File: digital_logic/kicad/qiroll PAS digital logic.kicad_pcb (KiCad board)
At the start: 2 copper layers, 26 parts, among them J1 led_sw1, J2 mode_thr_batt, J3 pas_sense, U1 14538, U2 4023, U3 4027, U4 14538, U5 L7805

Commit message: pcb version 1, new features
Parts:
- added C12: .1u, Capacitor_SMD:C_0603_1608Metric, F.Cu at (150.5, 55.9)
- added C13: .1u, Capacitor_SMD:C_0603_1608Metric, F.Cu at (144.8, 78.7)
- added H1: MountingHole_Pad, MountingHole:MountingHole_2.2mm_M2_DIN965_Pad, F.Cu at (162.1, 45.2)
- added H2: MountingHole_Pad, MountingHole:MountingHole_2.2mm_M2_DIN965_Pad, F.Cu at (113.8, 45.2)
- added H3: MountingHole_Pad, MountingHole:MountingHole_2.2mm_M2_DIN965_Pad, F.Cu at (162.1, 85.9)
- added H4: MountingHole_Pad, MountingHole:MountingHole_2.2mm_M2_DIN965_Pad, F.Cu at (113.8, 85.9)
- added J4: brk_sense, Connector_PinHeader_2.54mm:PinHeader_1x02_P2.54mm_Vertical, F.Cu at (156.8, 53.3)
- added J5: jumper, Connector_PinHeader_2.54mm:PinHeader_2x02_P2.54mm_Vertical, F.Cu at (133.3, 59.7)
- added R10: 1.6k, Resistor_SMD:R_0603_1608Metric, F.Cu at (118.7, 56.5)
- added R8: 100k, Resistor_SMD:R_0603_1608Metric, F.Cu at (117.5, 82.5)
- added R9: 392K, Resistor_SMD:R_0603_1608Metric, F.Cu at (131.4, 73.7)
- added U6: 4081, Package_SO:SOIC-14_3.9x8.7mm_P1.27mm, F.Cu at (144.8, 62.2)
- added U7: 4047, Package_SO:SOIC-14_3.9x8.7mm_P1.27mm, F.Cu at (124.5, 79.4)
- added U8: 74VHC1G32, Package_SO:TSOP-5_1.65x3.05mm_P0.95mm, F.Cu at (125.0, 68.6)
- C10: value .1u -> 0.47u
- C11: value .1u -> 1u
- C3, C4, C5: footprint Capacitor_SMD:C_0201_0603Metric -> Capacitor_SMD:C_0603_1608Metric
- C7: value 0.1u -> .1u
- C9: value 150u -> 200u; footprint Capacitor_THT:CP_Radial_D5.0mm_P2.00mm -> Capacitor_THT:CP_Radial_D6.3mm_P2.50mm
- J2: footprint Connector_Molex:Molex_KK-254_AE-6410-04A_1x04_P2.54mm_Vertical -> Connector_PinHeader_2.54mm:PinHeader_1x04_P2.54mm_Vertical
- J3: footprint Connector_Molex:Molex_KK-254_AE-6410-03A_1x03_P2.54mm_Vertical -> Connector_PinHeader_2.54mm:PinHeader_1x03_P2.54mm_Vertical
- U1, U3, U4: footprint Package_SO:TSSOP-16_4.4x5mm_P0.65mm -> Package_SO:SOIC-16_3.9x9.9mm_P1.27mm
- U2: footprint Package_SO:TSSOP-14_4.4x5mm_P0.65mm -> Package_SO:SOIC-14_3.9x8.7mm_P1.27mm
- moved C10 74.4 mm to (117.5, 78.1), turned to 180 degrees
- moved R3 62.0 mm to (141.6, 56.5)
- moved C11 59.4 mm to (131.4, 70.5), turned to 180 degrees
- moved R1 54.1 mm to (153.7, 56.5)
- moved C1 49.2 mm to (158.8, 56.5)
- moved R7 48.5 mm to (144.8, 80.6)
- moved U4 44.7 mm to (156.2, 78.7)
- moved R2 43.9 mm to (153.7, 71.1)
- moved R5 42.8 mm to (148.6, 80.6), turned to 180 degrees
- moved R6 42.5 mm to (158.8, 71.1)
- moved U2 41.7 mm to (134.0, 79.4), turned to 180 degrees
- moved U1 39.5 mm to (156.2, 62.9)
- moved R4 39.5 mm to (148.6, 83.2), turned to 180 degrees
- moved C4 38.8 mm to (158.8, 69.2), turned to 180 degrees
- moved C9 37.2 mm to (121.9, 60.3)
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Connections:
- C10 pad 1: GND -> Net-(C10-Pad1)
- C10 pad 2: VDD -> Net-(C10-Pad2)
- C11 pad 2: VDD -> Net-(C11-Pad2)
- C7 pad 1: VDD -> VCC
- C9 pad 1: VDD -> VCC
- J2 pad 2: Net-(C6-Pad1) -> Net-(J2-Pad2)
- J3 pad 1: VDD -> VCC
- R1 pad 1: VDD -> VCC
- R2 pad 1: VDD -> VCC
- R3 pad 1: VDD -> VCC
- R4 pad 1: VDD -> VCC
- R5 pad 1: VDD -> VCC
- R6 pad 1: VDD -> VCC
- U1 pad 13: VDD -> VCC
- U1 pad 16: VDD -> VCC
- U1 pad 3: VDD -> VCC
- U1 pad 5: VDD -> VCC
- U2 pad 1: Net-(U1-Pad10) -> Net-(U2-Pad1)
- U2 pad 10: Net-(U2-Pad10) -> Net-(U2-Pad1)
- U2 pad 11: Net-(J2-Pad3) -> BRK
- U2 pad 12: Net-(J2-Pad3) -> BRK
- U2 pad 13: Net-(J2-Pad3) -> BRK
- U2 pad 14: VDD -> VCC
- U2 pad 2: Net-(U1-Pad6) -> PEDAL
- U2 pad 8: Net-(J1-Pad3) -> PAS_ON
- U2 pad 9: Net-(J2-Pad3) -> Net-(R9-Pad2)
- U3 pad 1: Net-(J1-Pad3) -> PAS_ON
- U3 pad 10: VDD -> VCC
- U3 pad 11: VDD -> VCC
- U3 pad 12: Net-(U2-Pad10) -> PEDAL
- U3 pad 14: Net-(J2-Pad4) -> Net-(J5-Pad4)
- U3 pad 16: VDD -> VCC
- U3 pad 2: Net-(U3-Pad2) -> PAS_OFF
- U3 pad 5: VDD -> VCC
- U3 pad 6: VDD -> VCC
- U3 pad 9: GND -> BRK
- U4 pad 11: VDD -> VCC
- U4 pad 13: VDD -> VCC
- U4 pad 16: VDD -> VCC
- U4 pad 3: VDD -> VCC
- U5 pad 3: VDD -> VCC
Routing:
- net VCC: track 0.00 -> 241.8 mm, vias 0 -> 12
- net Net-(J1-Pad2): track 0.00 -> 85.7 mm, vias 0 -> 2
- net GND: track 0.00 -> 74.6 mm, vias 0 -> 18
- net PAS_OFF: track 0.00 -> 58.5 mm, vias 0 -> 6
- net Net-(U6-Pad3): track 0.00 -> 57.2 mm, vias 0 -> 4
- net BRK: track 0.00 -> 57.0 mm, vias 0 -> 4
- net Net-(U1-Pad10): track 0.00 -> 54.9 mm, vias 0 -> 2
- net Net-(J3-Pad3): track 0.00 -> 43.3 mm
- net RGN_FLSH: track 0.00 -> 39.6 mm, vias 0 -> 2
- net Net-(U2-Pad1): track 0.00 -> 39.5 mm, vias 0 -> 4
- net Net-(U6-Pad13): track 0.00 -> 35.0 mm, vias 0 -> 2
- net PAS_ON: track 0.00 -> 34.4 mm, vias 0 -> 2
- net PEDAL: track 0.00 -> 32.8 mm, vias 0 -> 4
- net Net-(J2-Pad3): track 0.00 -> 32.5 mm
- net Net-(U2-Pad5): track 0.00 -> 31.7 mm
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- added copper zone on B.Cu, net GND
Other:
- board outline added: 53.3 x 45.7 mm
- board text added: "+5v"
- board text added: "batt_in"
- board text added: "brk"
- board text added: "btn"
- board text added: "gnd"
- board text added: "led"
- board text added: "pedal"
- board text added: "pro/std"
- board text added: "qiroll pedal assist v1 Eric Dasmalchi"
- board text added: "rgn/ mode"
- board text added: "throttle"

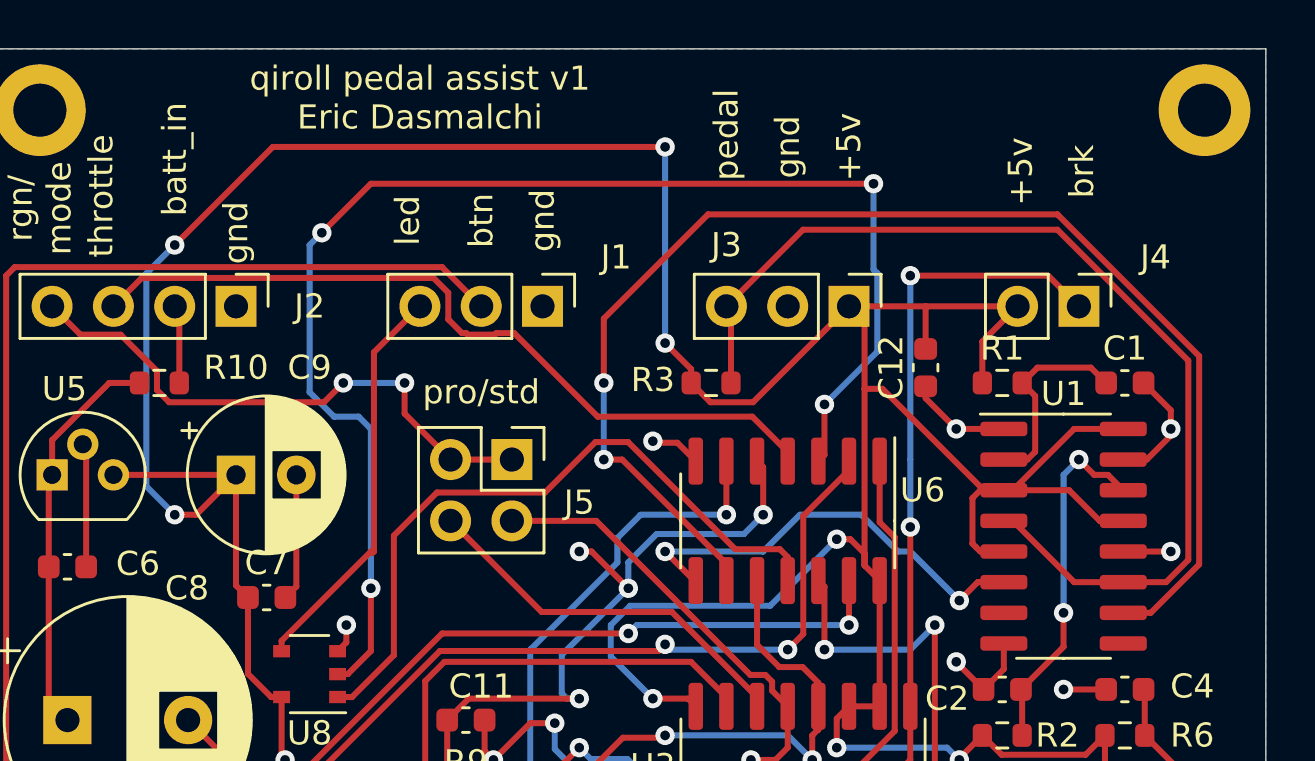
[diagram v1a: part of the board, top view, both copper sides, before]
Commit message: add brake sensor pulldown, incomplete BOM
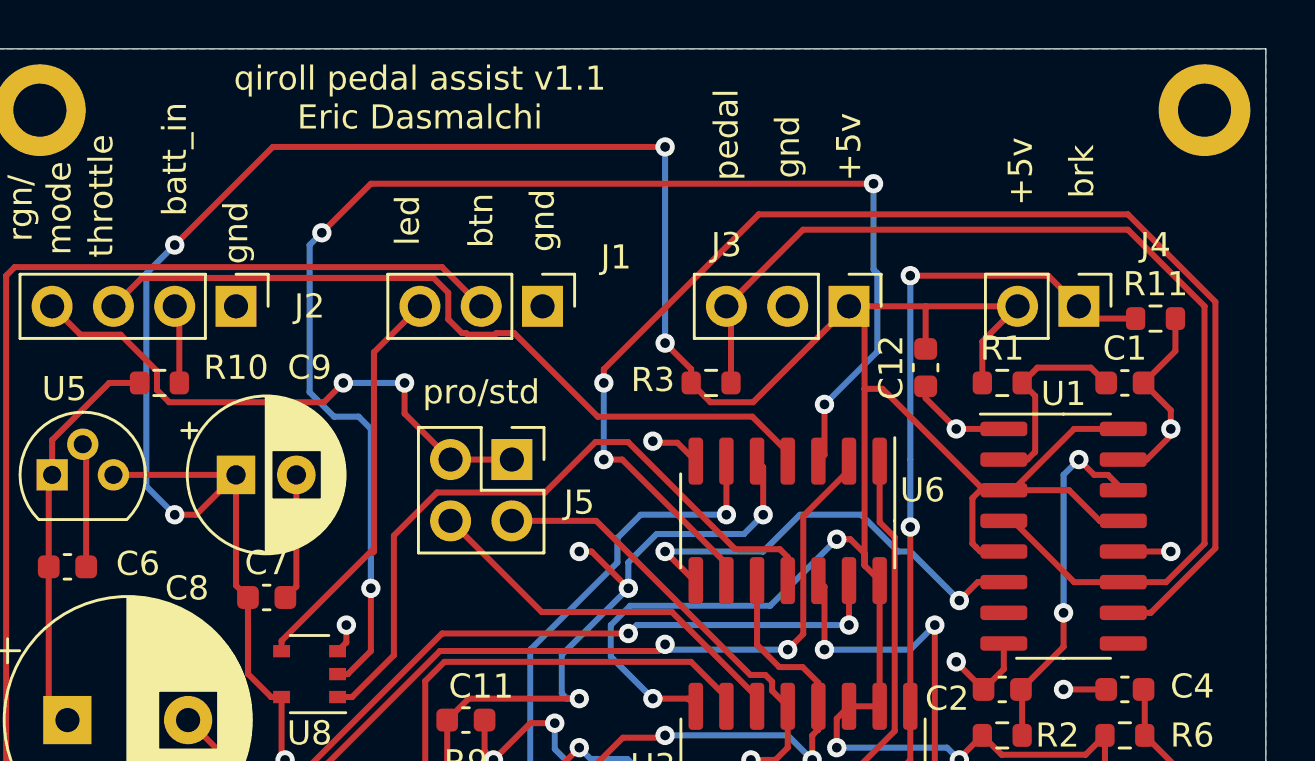
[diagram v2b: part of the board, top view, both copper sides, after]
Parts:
- added R11: 10k, Resistor_SMD:R_0603_1608Metric, F.Cu at (160.0, 53.8)
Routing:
- net GND: track 74.6 -> 77.8 mm
- net BRK: track 57.0 -> 59.6 mm
- net Net-(J3-Pad3): track 43.3 -> 45.6 mm
- net Net-(U1-Pad10): track 54.9 -> 55.9 mm
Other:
- board text added: "qiroll pedal assist v1.1 Eric Dasmalchi"
- board text removed: "qiroll pedal assist v1 Eric Dasmalchi"

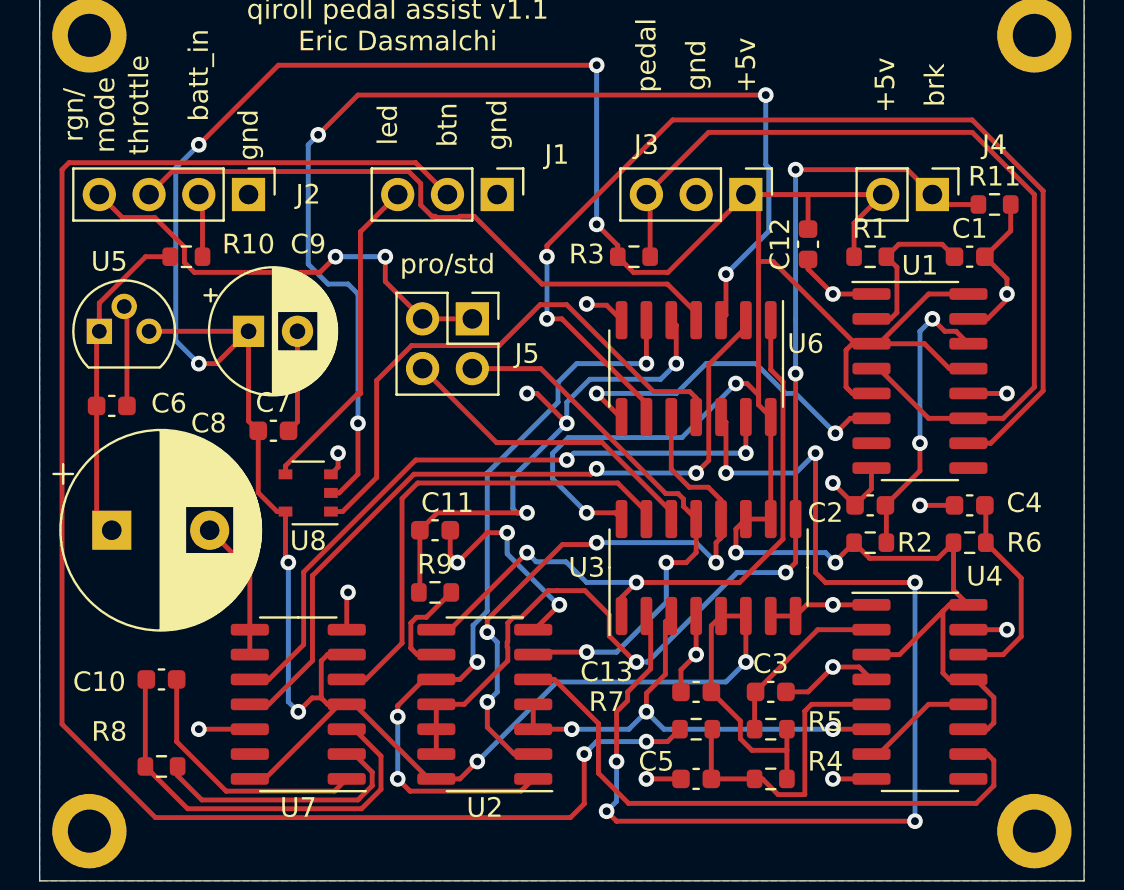
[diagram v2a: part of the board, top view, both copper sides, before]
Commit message: add ptc and protection diode for voltage reg
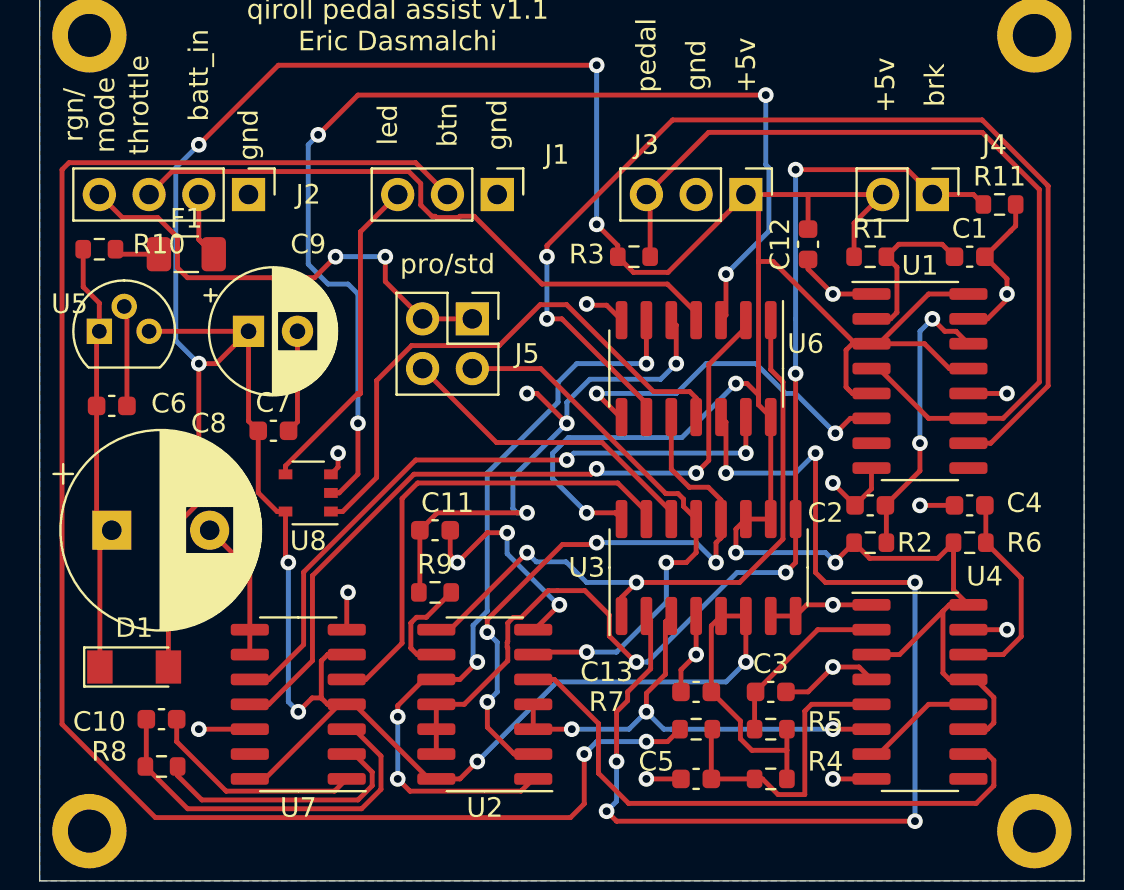
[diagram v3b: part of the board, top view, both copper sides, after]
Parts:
- added D1: Reverse Protect Diode, Diode_SMD:D_MiniMELF, F.Cu at (116.1, 77.5)
- added F1: PTC, Fuse:Fuse_1206_3216Metric, F.Cu at (118.7, 56.4)
- moved R10 4.46 mm to (114.3, 56.1)
- moved C10 2.03 mm to (117.5, 80.1)
- moved R11 0.25 mm to (160.3, 53.8)
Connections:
- J2 pad 2: Net-(J2-Pad2) -> Net-(F1-Pad2)
- R10 pad 2: Net-(J2-Pad2) -> Net-(F1-Pad1)
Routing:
- net VCC: track 241.8 -> 257.9 mm
- net Net-(C6-Pad1): track 16.6 -> 22.3 mm
- net Net-(F1-Pad2): track 0.00 -> 4.35 mm
- net Net-(J2-Pad2): track 3.25 -> 0.00 mm
- net Net-(F1-Pad1): track 0.00 -> 2.32 mm
- net Net-(C10-Pad1): track 13.2 -> 11.1 mm
- net Net-(C10-Pad2): track 21.8 -> 19.9 mm
- net BRK: track 59.6 -> 60.5 mm
- net Net-(J2-Pad4): track 23.5 -> 24.2 mm
- net Net-(J3-Pad3): track 45.6 -> 46.1 mm
- net Net-(U1-Pad10): track 55.9 -> 56.5 mm

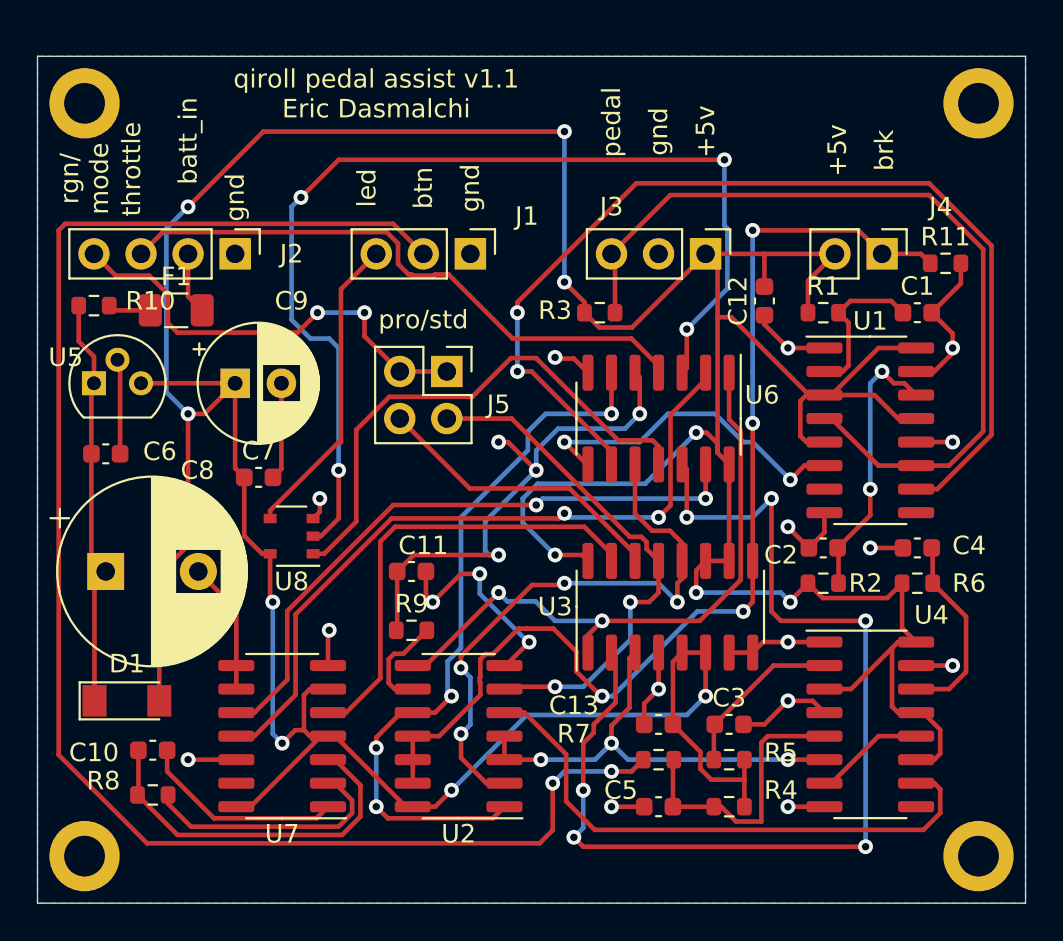
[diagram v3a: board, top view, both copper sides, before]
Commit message: revised pcb w/ ptc, protection diode, revised c11 value
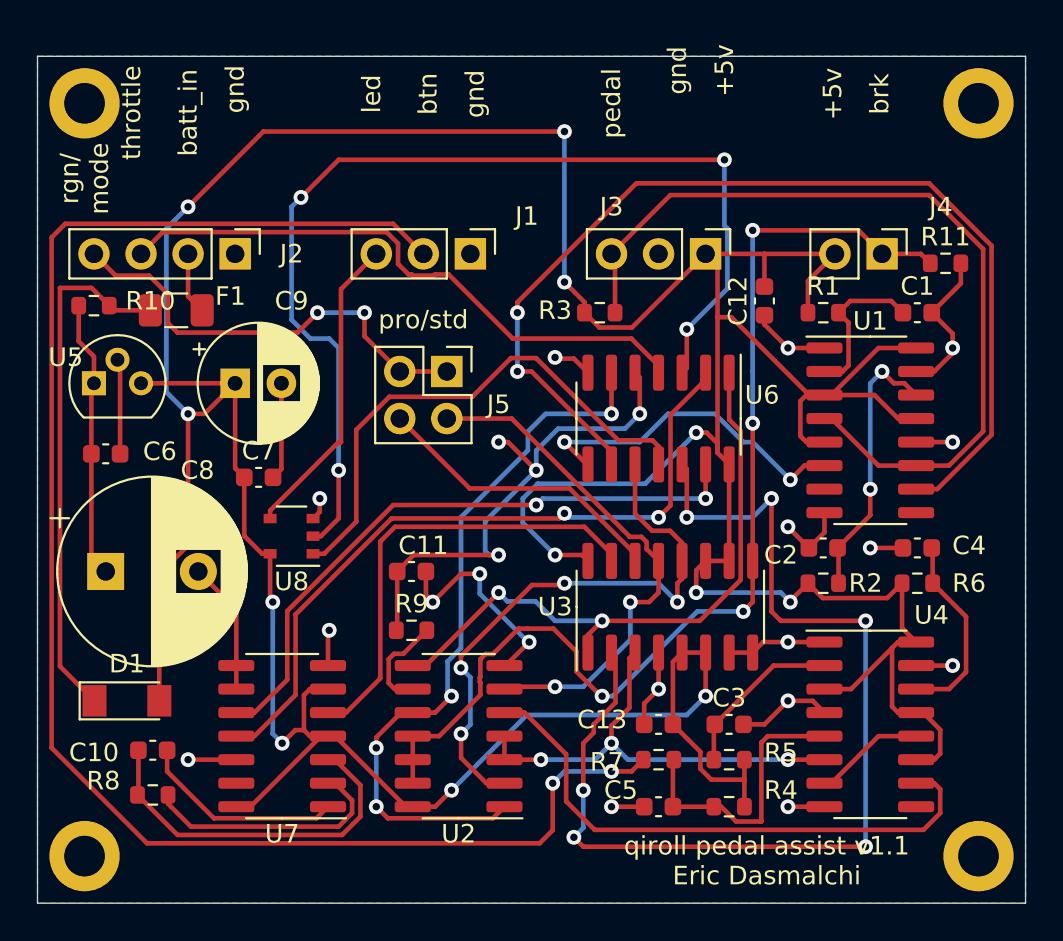
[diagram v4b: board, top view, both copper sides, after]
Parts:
- C11: value 1u -> .1u
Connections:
- D1 pad 1: Net-(C6-Pad1) -> Net-(D1-Pad1)
- F1 pad 1: Net-(F1-Pad1) -> Net-(D1-Pad1)
- R10 pad 2: Net-(F1-Pad1) -> Net-(D1-Pad1)
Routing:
- net Net-(D1-Pad1): track 0.00 -> 28.4 mm
- net Net-(C6-Pad1): track 22.3 -> 15.9 mm
- net Net-(F1-Pad1): track 2.32 -> 0.00 mm
